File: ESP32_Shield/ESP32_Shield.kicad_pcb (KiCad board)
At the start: 2 copper layers, 65.8 x 89.1 mm, 31 parts, among them J1 Conn_01x19_Female, J2 Conn_01x19_Female, J3 Conn_01x19_Female, J4 Conn_01x19_Female, J5 Screw_Terminal_01x03, J6 Screw_Terminal_01x03, J7 Screw_Terminal_01x03, K1 FINDER-36.11, K2 FINDER-36.11, K3 FINDER-36.11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

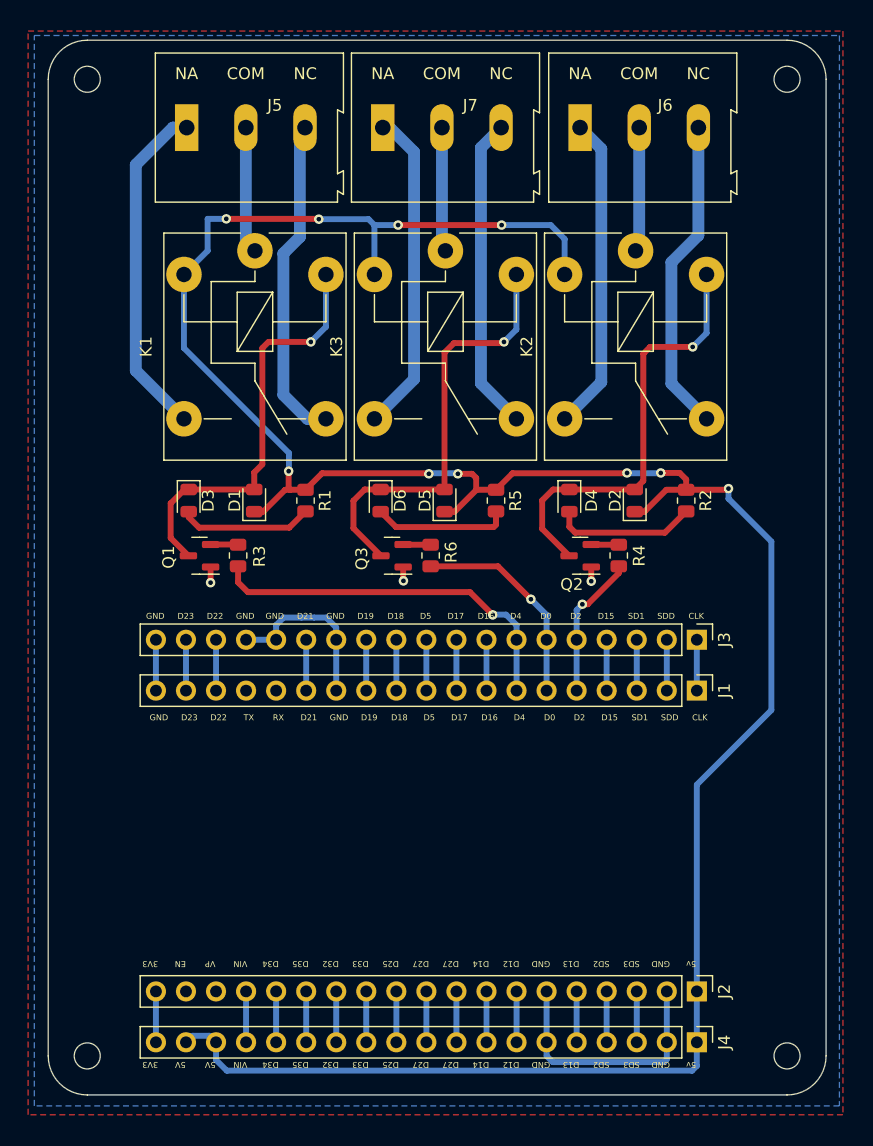
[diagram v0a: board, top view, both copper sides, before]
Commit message: PCB: added the last power plane
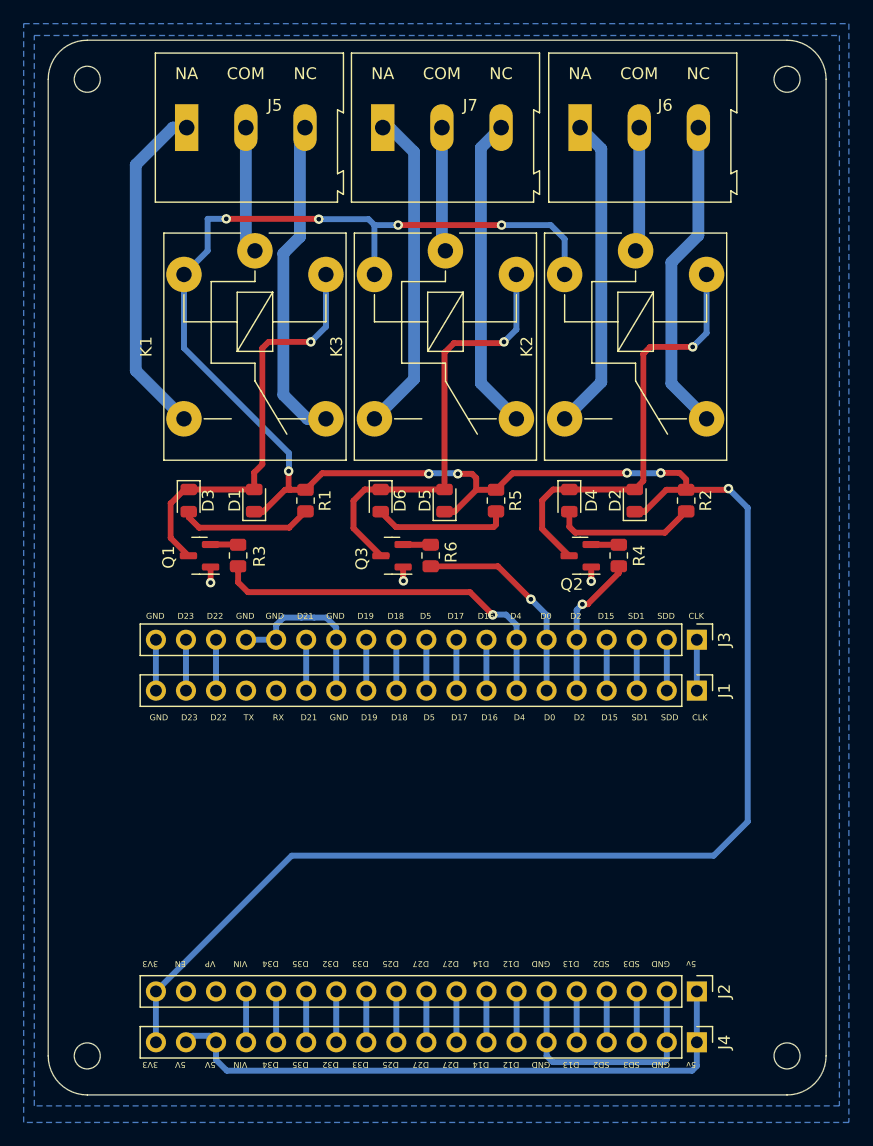
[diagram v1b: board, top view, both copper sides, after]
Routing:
- net +5V: track 0.00 -> 52.0 mm
- net +3.3V: track 221.3 -> 207.5 mm
- removed copper zone on F.Cu, net +3.3V
